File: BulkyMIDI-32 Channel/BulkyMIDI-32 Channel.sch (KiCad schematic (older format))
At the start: 120 parts, among them J1 DC IN, J2 MIDI THRU, J3 MIDI IN, J4 Panel, M1 Mounting, M2 Mounting, M3 Mounting, M4 Mounting, Q1 2N3906, Q10 2N3904, Q11 2N3904, Q12 2N3904, Q13 2N3904, Q14 2N3904, Q15 2N3904, Q16 2N3904, Q17 2N3904, Q2 2N3904, Q3 2N3904, Q4 2N3904, Q5 2N3904, Q6 2N3904, Q7 2N3904, Q8 2N3904, Q9 2N3904, U1 CD4009, U2 CD4081, U3 6N138, U4 CD4023, U5 CD4040, U6 CD4017, U7 CD4094, U8 CD4514, Y1 4Mhz

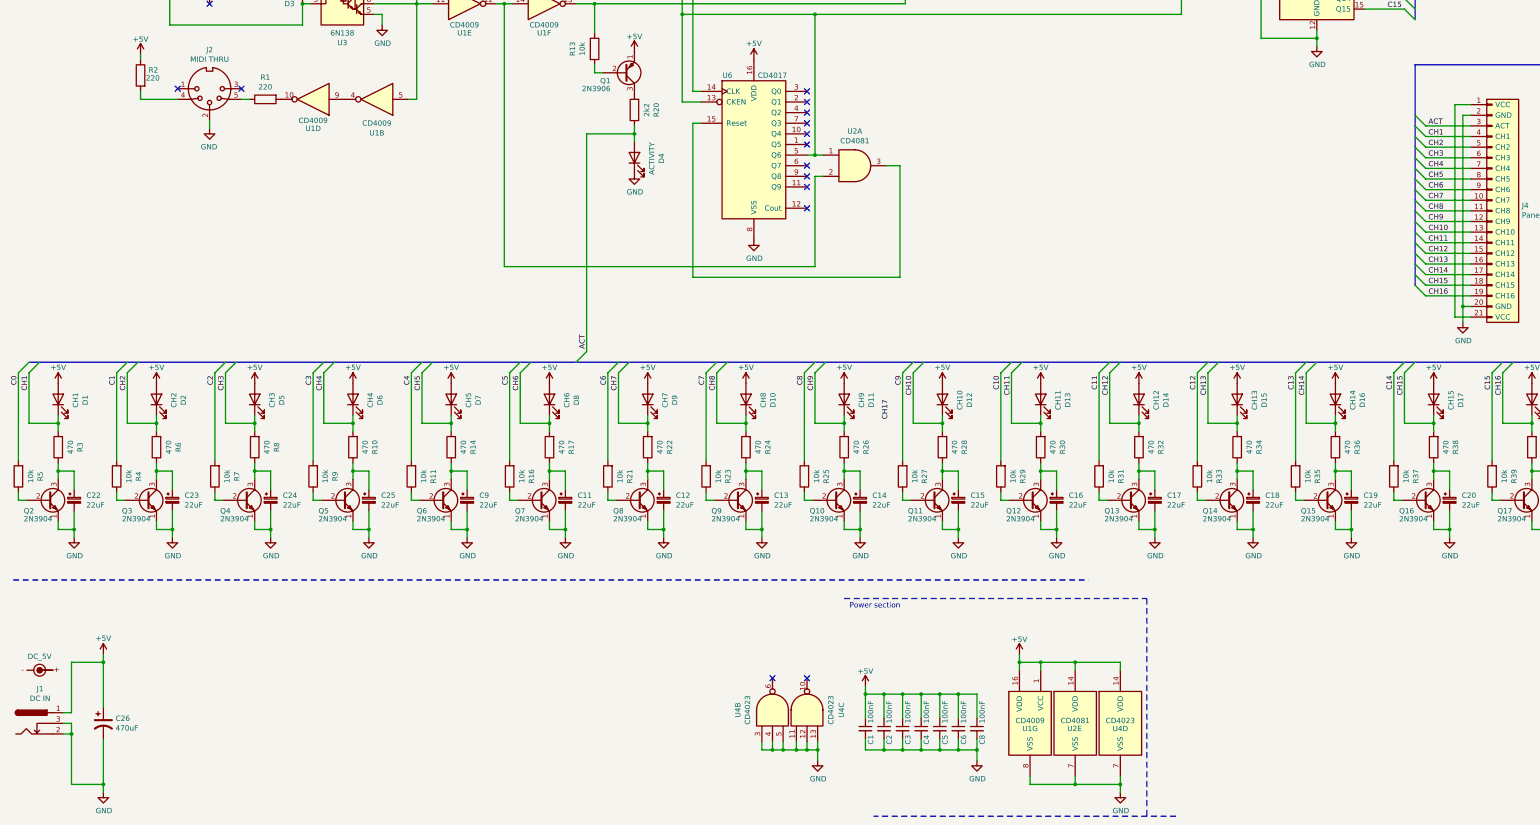
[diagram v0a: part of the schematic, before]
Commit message: Added channel front panel
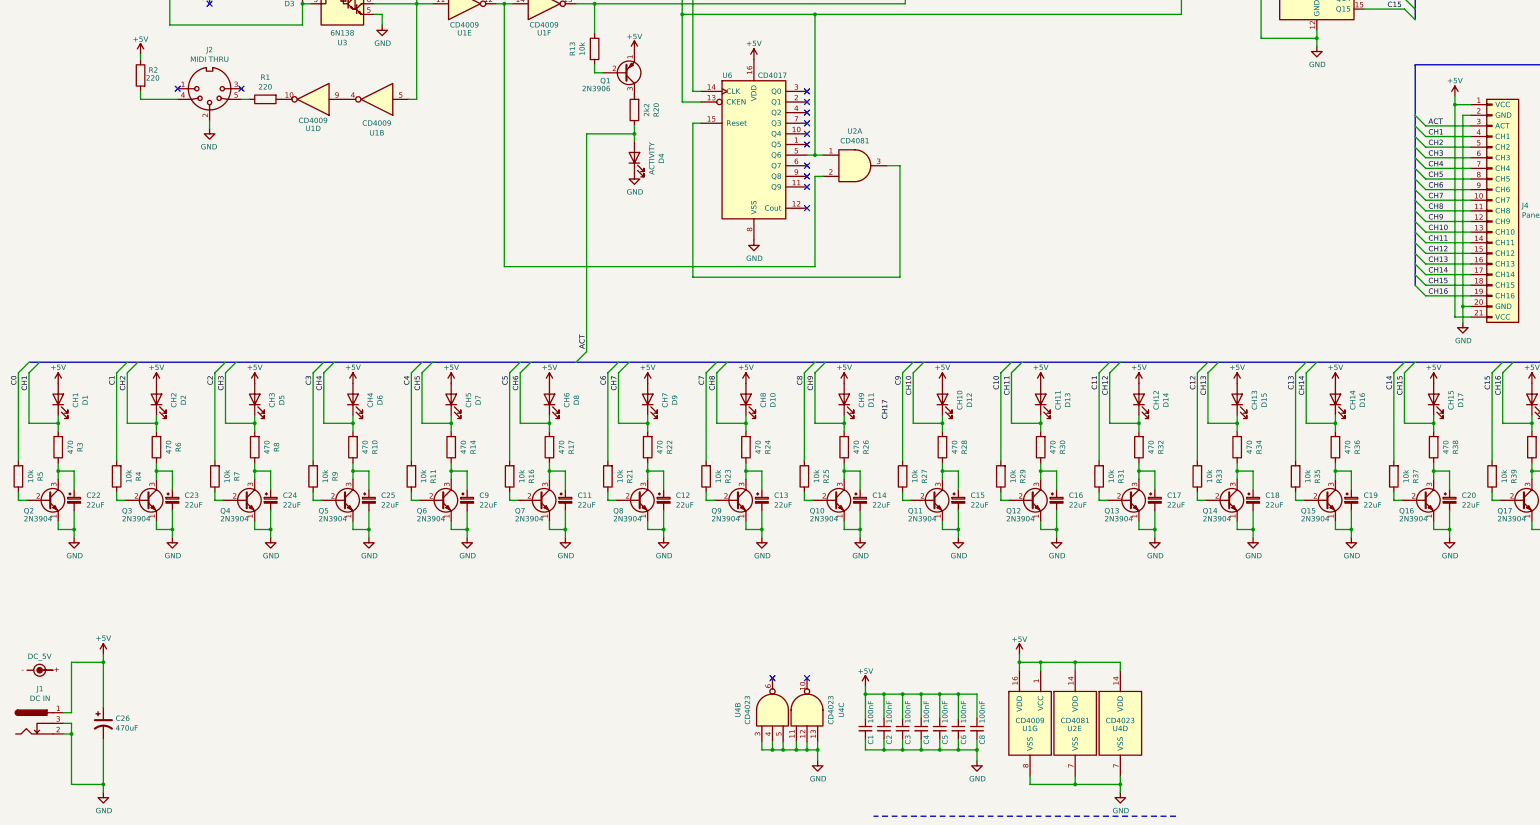
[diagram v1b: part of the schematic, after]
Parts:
- D1, D10, D11, D12, D13, D14, D15, D16, D17, D18, D2, D4, D5, D6, D7, D8, D9: footprint LED_THT:LED_D5.0mm_Horizontal_O1.27mm_Z3.0mm -> LED_THT:LED_D3.0mm
- U1: footprint Package_DIP:DIP-14_W7.62mm_Socket_LongPads -> Package_DIP:DIP-16_W7.62mm_Socket_LongPads
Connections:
- net +5V: now also J4.1 (VCC), J4.21 (VCC)
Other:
- note removed: "Power section"
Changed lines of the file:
@@
 	1    0    0    -1
 $EndComp
-Text Notes 8875 9175 0    50   ~ 0
-Power section
 Wire Wire Line
 	2850 4575 2850 4650
@@
 Connection ~ 4800 3475
 Wire Notes Line
-	8825 9075 11675 9075
-Wire Notes Line
-	11675 9075 11675 11125
-Wire Notes Line
 	11950 11125 9100 11125
 Wire Wire Line
@@
 F 0 "D4" H 6843 4670 50  0000 C CNN
 F 1 "ACTIVITY" H 6843 4761 50  0000 C CNN
-F 2 "LED_THT:LED_D5.0mm_Horizontal_O1.27mm_Z3.0mm" H 6850 4925 50  0001 C CNN
+F 2 "LED_THT:LED_D3.0mm" H 6850 4925 50  0001 C CNN
 F 3 "~" H 6850 4925 50  0001 C CNN
 	1    6850 4925
@@
 F 0 "U1" H 6425 1825 50  0000 C CNN
 F 1 "CD4009" H 6425 1750 50  0000 C CNN
-F 2 "Package_DIP:DIP-14_W7.62mm_Socket_LongPads" H 6425 1525 50  0001 C CNN
+F 2 "Package_DIP:DIP-16_W7.62mm_Socket_LongPads" H 6425 1525 50  0001 C CNN
 F 3 "http://www.ti.com/lit/gpn/sn74HC14" H 6425 1525 50  0001 C CNN
 	1    6425 1525
@@
 F 0 "U1" H 4425 4692 50  0000 C CNN
 F 1 "CD4009" H 4425 4600 50  0000 C CNN
-F 2 "Package_DIP:DIP-14_W7.62mm_Socket_LongPads" H 4425 4375 50  0001 C CNN
+F 2 "Package_DIP:DIP-16_W7.62mm_Socket_LongPads" H 4425 4375 50  0001 C CNN
 F 3 "http://www.ti.com/lit/gpn/sn74HC14" H 4425 4375 50  0001 C CNN
 	2    4425 4375
@@
 F 0 "U1" H 10575 10200 50  0000 C CNN
 F 1 "CD4009" H 10575 10275 50  0000 C CNN
-F 2 "Package_DIP:DIP-14_W7.62mm_Socket_LongPads" H 10575 10250 50  0001 C CNN
+F 2 "Package_DIP:DIP-16_W7.62mm_Socket_LongPads" H 10575 10250 50  0001 C CNN
 F 3 "http://www.ti.com/lit/gpn/sn74HC14" H 10575 10250 50  0001 C CNN
 	7    10575 10250
@@
 F 0 "U1" H 6000 3200 50  0000 C CNN
 F 1 "CD4009" H 6000 3275 50  0000 C CNN
-F 2 "Package_DIP:DIP-14_W7.62mm_Socket_LongPads" H 6000 3475 50  0001 C CNN
+F 2 "Package_DIP:DIP-16_W7.62mm_Socket_LongPads" H 6000 3475 50  0001 C CNN
 F 3 "http://www.ti.com/lit/gpn/sn74HC14" H 6000 3475 50  0001 C CNN
 	6    6000 3475
@@
 F 0 "U1" H 5250 3200 50  0000 C CNN
 F 1 "CD4009" H 5250 3275 50  0000 C CNN
-F 2 "Package_DIP:DIP-14_W7.62mm_Socket_LongPads" H 5250 3475 50  0001 C CNN
+F 2 "Package_DIP:DIP-16_W7.62mm_Socket_LongPads" H 5250 3475 50  0001 C CNN
 F 3 "http://www.ti.com/lit/gpn/sn74HC14" H 5250 3475 50  0001 C CNN
 	5    5250 3475
@@
 F 0 "U1" H 7175 1825 50  0000 C CNN
 F 1 "CD4009" H 7175 1750 50  0000 C CNN
-F 2 "Package_DIP:DIP-14_W7.62mm_Socket_LongPads" H 7175 1525 50  0001 C CNN
+F 2 "Package_DIP:DIP-16_W7.62mm_Socket_LongPads" H 7175 1525 50  0001 C CNN
 F 3 "http://www.ti.com/lit/gpn/sn74HC14" H 7175 1525 50  0001 C CNN
 	3    7175 1525
@@
 F 0 "U1" H 3825 4650 50  0000 C CNN
 F 1 "CD4009" H 3825 4575 50  0000 C CNN
-F 2 "Package_DIP:DIP-14_W7.62mm_Socket_LongPads" H 3825 4375 50  0001 C CNN
+F 2 "Package_DIP:DIP-16_W7.62mm_Socket_LongPads" H 3825 4375 50  0001 C CNN
 F 3 "http://www.ti.com/lit/gpn/sn74HC14" H 3825 4375 50  0001 C CNN
 	4    3825 4375
@@
 Wire Wire Line
 	10675 9675 10675 9750
-Wire Notes Line
-	1000 8900 11125 8900
 Wire Wire Line
 	8050 10425 8050 10500
@@
 F 0 "D10" H 7893 6945 50  0000 C CNN
 F 1 "CH8" H 7893 7036 50  0000 C CNN
-F 2 "LED_THT:LED_D5.0mm_Horizontal_O1.27mm_Z3.0mm" H 7900 7200 50  0001 C CNN
+F 2 "LED_THT:LED_D3.0mm" H 7900 7200 50  0001 C CNN
 F 3 "~" H 7900 7200 50  0001 C CNN
 	1    7900 7200
@@
 F 0 "D11" H 8818 6945 50  0000 C CNN
 F 1 "CH9" H 8818 7036 50  0000 C CNN
-F 2 "LED_THT:LED_D5.0mm_Horizontal_O1.27mm_Z3.0mm" H 8825 7200 50  0001 C CNN
+F 2 "LED_THT:LED_D3.0mm" H 8825 7200 50  0001 C CNN
 F 3 "~" H 8825 7200 50  0001 C CNN
 	1    8825 7200
@@
 F 0 "D12" H 9743 6945 50  0000 C CNN
 F 1 "CH10" H 9743 7036 50  0000 C CNN
-F 2 "LED_THT:LED_D5.0mm_Horizontal_O1.27mm_Z3.0mm" H 9750 7200 50  0001 C CNN
+F 2 "LED_THT:LED_D3.0mm" H 9750 7200 50  0001 C CNN
 F 3 "~" H 9750 7200 50  0001 C CNN
 	1    9750 7200
@@
 F 0 "D13" H 10668 6945 50  0000 C CNN
 F 1 "CH11" H 10668 7036 50  0000 C CNN
-F 2 "LED_THT:LED_D5.0mm_Horizontal_O1.27mm_Z3.0mm" H 10675 7200 50  0001 C CNN
+F 2 "LED_THT:LED_D3.0mm" H 10675 7200 50  0001 C CNN
 F 3 "~" H 10675 7200 50  0001 C CNN
 	1    10675 7200
@@
 F 0 "D14" H 11593 6945 50  0000 C CNN
 F 1 "CH12" H 11593 7036 50  0000 C CNN
-F 2 "LED_THT:LED_D5.0mm_Horizontal_O1.27mm_Z3.0mm" H 11600 7200 50  0001 C CNN
+F 2 "LED_THT:LED_D3.0mm" H 11600 7200 50  0001 C CNN
 F 3 "~" H 11600 7200 50  0001 C CNN
 	1    11600 7200
@@
 F 0 "D15" H 12518 6945 50  0000 C CNN
 F 1 "CH13" H 12518 7036 50  0000 C CNN
-F 2 "LED_THT:LED_D5.0mm_Horizontal_O1.27mm_Z3.0mm" H 12525 7200 50  0001 C CNN
+F 2 "LED_THT:LED_D3.0mm" H 12525 7200 50  0001 C CNN
 F 3 "~" H 12525 7200 50  0001 C CNN
 	1    12525 7200
@@
 F 0 "D16" H 13443 6945 50  0000 C CNN
 F 1 "CH14" H 13443 7036 50  0000 C CNN
-F 2 "LED_THT:LED_D5.0mm_Horizontal_O1.27mm_Z3.0mm" H 13450 7200 50  0001 C CNN
+F 2 "LED_THT:LED_D3.0mm" H 13450 7200 50  0001 C CNN
 F 3 "~" H 13450 7200 50  0001 C CNN
 	1    13450 7200
@@
 F 0 "D17" H 14368 6945 50  0000 C CNN
 F 1 "CH15" H 14368 7036 50  0000 C CNN
-F 2 "LED_THT:LED_D5.0mm_Horizontal_O1.27mm_Z3.0mm" H 14375 7200 50  0001 C CNN
+F 2 "LED_THT:LED_D3.0mm" H 14375 7200 50  0001 C CNN
 F 3 "~" H 14375 7200 50  0001 C CNN
 	1    14375 7200
@@
 F 0 "D18" H 15293 6945 50  0000 C CNN
 F 1 "CH16" H 15293 7036 50  0000 C CNN
-F 2 "LED_THT:LED_D5.0mm_Horizontal_O1.27mm_Z3.0mm" H 15300 7200 50  0001 C CNN
+F 2 "LED_THT:LED_D3.0mm" H 15300 7200 50  0001 C CNN
 F 3 "~" H 15300 7200 50  0001 C CNN
 	1    15300 7200
@@
 F 0 "D9" H 6968 6945 50  0000 C CNN
 F 1 "CH7" H 6968 7036 50  0000 C CNN
-F 2 "LED_THT:LED_D5.0mm_Horizontal_O1.27mm_Z3.0mm" H 6975 7200 50  0001 C CNN
+F 2 "LED_THT:LED_D3.0mm" H 6975 7200 50  0001 C CNN
 F 3 "~" H 6975 7200 50  0001 C CNN
 	1    6975 7200
@@
 F 0 "D8" H 6043 6945 50  0000 C CNN
 F 1 "CH6" H 6043 7036 50  0000 C CNN
-F 2 "LED_THT:LED_D5.0mm_Horizontal_O1.27mm_Z3.0mm" H 6050 7200 50  0001 C CNN
+F 2 "LED_THT:LED_D3.0mm" H 6050 7200 50  0001 C CNN
 F 3 "~" H 6050 7200 50  0001 C CNN
 	1    6050 7200
@@
 F 0 "D7" H 5118 6945 50  0000 C CNN
 F 1 "CH5" H 5118 7036 50  0000 C CNN
-F 2 "LED_THT:LED_D5.0mm_Horizontal_O1.27mm_Z3.0mm" H 5125 7200 50  0001 C CNN
+F 2 "LED_THT:LED_D3.0mm" H 5125 7200 50  0001 C CNN
 F 3 "~" H 5125 7200 50  0001 C CNN
 	1    5125 7200
@@
 F 0 "D6" H 4193 6945 50  0000 C CNN
 F 1 "CH4" H 4193 7036 50  0000 C CNN
-F 2 "LED_THT:LED_D5.0mm_Horizontal_O1.27mm_Z3.0mm" H 4200 7200 50  0001 C CNN
+F 2 "LED_THT:LED_D3.0mm" H 4200 7200 50  0001 C CNN
 F 3 "~" H 4200 7200 50  0001 C CNN
 	1    4200 7200
@@
 F 0 "D5" H 3268 6945 50  0000 C CNN
 F 1 "CH3" H 3268 7036 50  0000 C CNN
-F 2 "LED_THT:LED_D5.0mm_Horizontal_O1.27mm_Z3.0mm" H 3275 7200 50  0001 C CNN
+F 2 "LED_THT:LED_D3.0mm" H 3275 7200 50  0001 C CNN
 F 3 "~" H 3275 7200 50  0001 C CNN
 	1    3275 7200
@@
 F 0 "D2" H 2343 6945 50  0000 C CNN
 F 1 "CH2" H 2343 7036 50  0000 C CNN
-F 2 "LED_THT:LED_D5.0mm_Horizontal_O1.27mm_Z3.0mm" H 2350 7200 50  0001 C CNN
+F 2 "LED_THT:LED_D3.0mm" H 2350 7200 50  0001 C CNN
 F 3 "~" H 2350 7200 50  0001 C CNN
 	1    2350 7200
@@
 F 0 "D1" H 1418 6945 50  0000 C CNN
 F 1 "CH1" H 1418 7036 50  0000 C CNN
-F 2 "LED_THT:LED_D5.0mm_Horizontal_O1.27mm_Z3.0mm" H 1425 7200 50  0001 C CNN
+F 2 "LED_THT:LED_D3.0mm" H 1425 7200 50  0001 C CNN
 F 3 "~" H 1425 7200 50  0001 C CNN
 	1    1425 7200
@@
 Wire Bus Line
 	15825 4050 15825 1700
+$Comp
+L power:+5V #PWR?
+U 1 1 667AD9AD
+P 14575 4350
+F 0 "#PWR?" H 14575 4200 50  0001 C CNN
+F 1 "+5V" H 14575 4500 50  0000 C CNN
+F 2 "" H 14575 4350 50  0001 C CNN
+F 3 "" H 14575 4350 50  0001 C CNN
+	1    14575 4350
+	1    0    0    -1
+$EndComp
+Wire Wire Line
+	14575 4350 14575 4425
+Connection ~ 14575 4425
 Wire Bus Line
 	14200 4050 14200 6125

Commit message: Untested VU SIDI module
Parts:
- added J5: Conn_Power, BulkyMIDI-32:Conn_Power, symbol BulkyMIDI:Conn_Power
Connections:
- net +5V: now also J5.1 (VCC)
- net GND: now also J5.2 (GND)
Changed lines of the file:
@@
 	15825 4050 15825 1700
 $Comp
-L power:+5V #PWR?
+L power:+5V #PWR01
 U 1 1 667AD9AD
 P 14575 4350
-F 0 "#PWR?" H 14575 4200 50  0001 C CNN
+F 0 "#PWR01" H 14575 4200 50  0001 C CNN
 F 1 "+5V" H 14575 4500 50  0000 C CNN
 F 2 "" H 14575 4350 50  0001 C CNN
@@
 	14575 4350 14575 4425
 Connection ~ 14575 4425
+$Comp
+L BulkyMIDI:Conn_Power J5
+U 1 1 628A1490
+P 2500 10200
+F 0 "J5" H 2803 10196 50  0000 L CNN
+F 1 "Conn_Power" H 2803 10105 50  0000 L CNN
+F 2 "BulkyMIDI-32:Conn_Power" H 2500 10200 50  0001 C CNN
+F 3 "~" H 2500 10200 50  0001 C CNN
+	1    2500 10200
+	1    0    0    -1
+$EndComp
+Wire Wire Line
+	2300 10200 2225 10200
+Wire Wire Line
+	2225 10200 2225 9675
+Wire Wire Line
+	2225 9675 1850 9675
+Wire Wire Line
+	2300 10300 2225 10300
+Wire Wire Line
+	2225 10300 2225 10825
+Wire Wire Line
+	2225 10825 1850 10825
 Wire Bus Line
 	14200 4050 14200 6125

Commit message: Wrong capacitor value
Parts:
- C10, C27: value 68nF -> 68pF
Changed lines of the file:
@@
 P 6050 2550
 F 0 "C27" H 6150 2600 50  0000 L CNN
-F 1 "68nF" H 6150 2525 50  0000 L CNN
+F 1 "68pF" H 6150 2525 50  0000 L CNN
 F 2 "Capacitor_THT:C_Disc_D4.7mm_W2.5mm_P5.00mm" H 6050 2550 50  0001 C CNN
 F 3 "~" H 6050 2550 50  0001 C CNN
@@
 P 6800 2550
 F 0 "C10" H 6900 2500 50  0000 L CNN
-F 1 "68nF" H 6900 2575 50  0000 L CNN
+F 1 "68pF" H 6900 2575 50  0000 L CNN
 F 2 "Capacitor_THT:C_Disc_D4.7mm_W2.5mm_P5.00mm" H 6800 2550 50  0001 C CNN
 F 3 "~" H 6800 2550 50  0001 C CNN
